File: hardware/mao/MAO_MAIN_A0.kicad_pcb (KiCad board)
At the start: 4 copper layers, 58 x 55.4 mm, 142 parts, among them J101 USB-C, J102 BAT, J201 TAG, J301 LCD, J302 TOUCH TOP, J303 TOUCH REAR, J501 LRA, Q101 AO3401A, Q501 AO3400A, SW301 SKQGADE010, U101 TPD2E2U06, U102 BQ24073RGTR, U103 MAX17048G+T10, U104 TPS63802DLAR, U105 TPS22919DCKR, U201 ESP32-S3-WROOM-1-N8R2, U202 TCA6408ARGTR, U301 DRV5012AEDMRR, U302 DRV5012AEDMRR, U303 AW9364DNR, U401 LSM6DSOXTR, U402 VL53L4CDV0DH/1, U403 OPT3004DNPR, U501 MAX98357AETE+T, U502 DRV2605LDGSR, U503 IRM-H638T/TR2

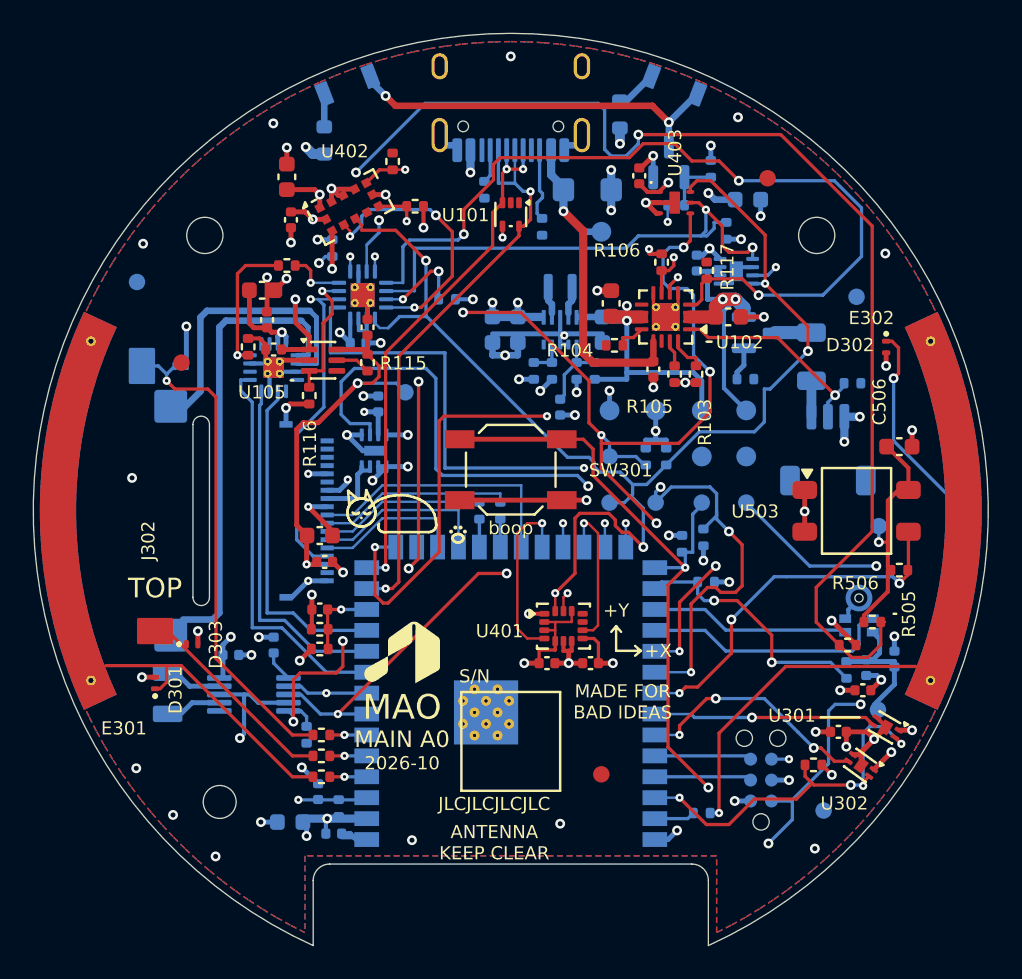
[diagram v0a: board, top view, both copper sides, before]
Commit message: MAO A0 final pass: rebuilt board, panel clock option, doc numbers from the final board
Board (rebuilt from design/, DRC 0 / 0 unconnected / parity 0, planes one piece, silk 0, mech 0):
- silk leaders at least one text height (0.8 mm) long; shorter ones read as dashes
- VSYS via at R502 on the pad's axis: every segment at 0/45/90 degrees
- FAB-NOTES notch size generated from mechanical.py (24.0 mm wide, 7.55 mm deep)
- antenna keep-out comments describe what the rule area really covers

Firmware:
- Kconfig MAO_A0_LCD_PCLK_MHZ (10-80, default 80) for the panel SPI clock through the 70 mm tail
- pin map: BOARD_ID routing note; header regenerated
- all five configurations build with 0 warnings; host tests 240 checks pass

Docs: power budget (EN1 strap 11 uA, deep sleep ~85 uA), mechanical (module datum, notch, wall test,
tabs, tail loop and well, LRA), architecture section 6, factory-test pad positions, firmware merge guide
(clock option, reconfigure note), simulation labels (S3 66 mW at 47 mA, S10 t_ON vs rise, S15 deep sleep),
renders, layer plots, Gerber sheet and assembly previews regenerated.

Co-Authored-By: Claude Opus 5.5 <noreply@anthropic.com>
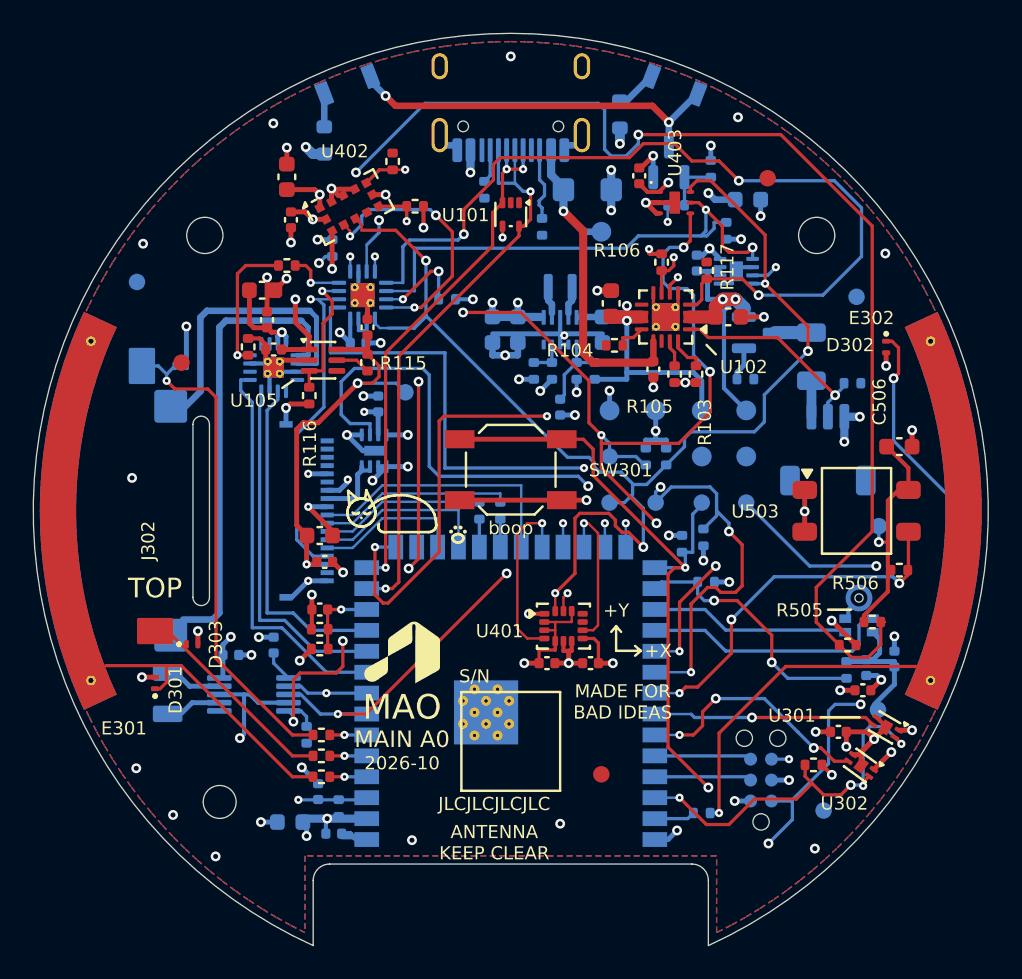
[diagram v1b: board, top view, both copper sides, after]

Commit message: MAO A0 service field: every name upright beside its pad; review and verification docs updated
- mechanical.field_name_box sized to the real glyphs (0.72 mm a character): the router no longer puts a
  via where a name has to go (BOOT was pushed off its pad by one)
- silk.py: field names may use a neighbour's courtyard margin (never its body or pads); the field
  search gets a lower bound and finds the optimum at once (an all-upright set was proved impossible
  before the keep-out change: SYS lay flat)
- check_silk_text.py: the same body rule for field names; findings carry their own position
- TP9's name box slid 0.05 mm clear of the module escape via of LCD_BL_CTRL
- final board: DRC 0 / 0 / parity 0, planes one piece, silk 84 texts 0 findings, mech 0;
  208 vias, 930 segments all on 45 degrees, L3/L4 broadside 17.4 mm
- review: schematic rows (ILIM, GPIO45, board ID), audit-2 change rows 41-52, PCB gates and metrics,
  ODD JOBS and order-readiness rows; verification: summary, S3/S10/S15, second-round section;
  type scale corrected (references 0.8 mm); renders, plots, Gerber sheet regenerated

Co-Authored-By: Claude Opus 5.5 <noreply@anthropic.com>
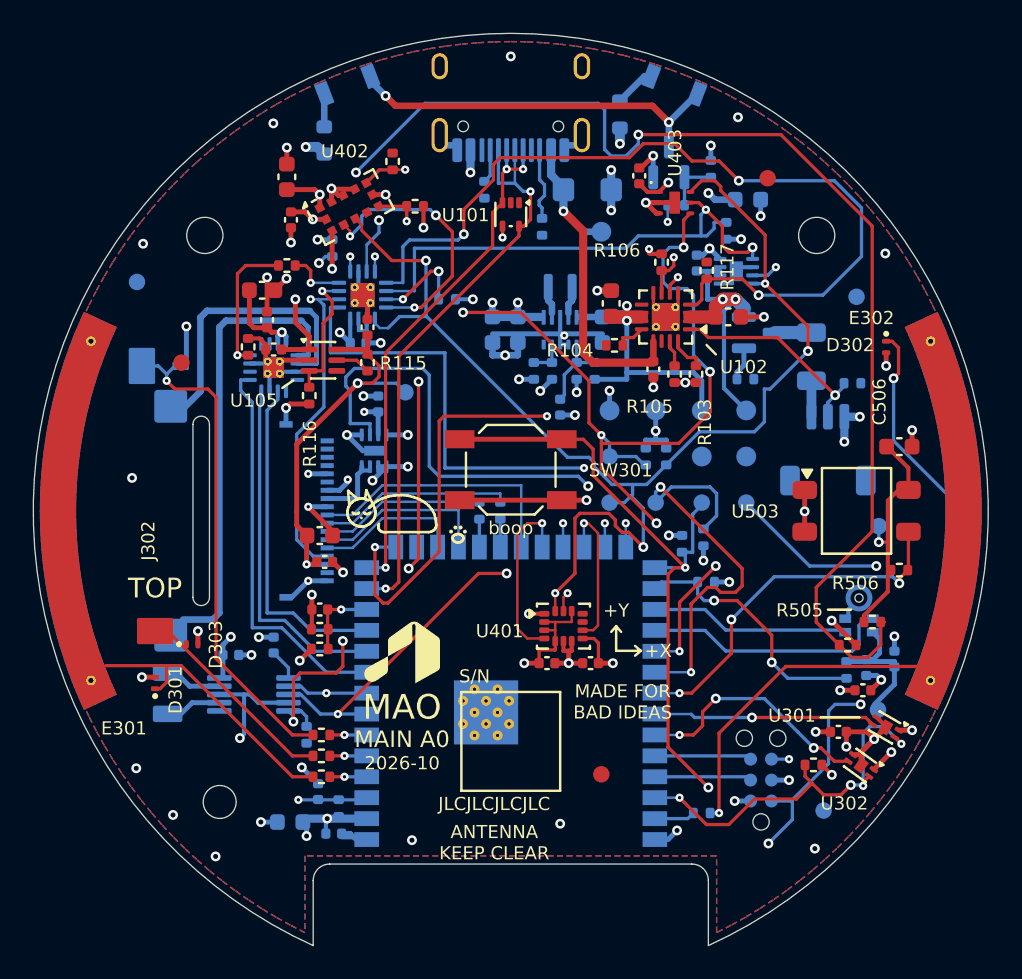
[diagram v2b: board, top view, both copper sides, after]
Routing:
- net EXP_RST_N: track 53.9 -> 56.8 mm, vias 4 -> 3
- net 3V3_LCD: track 24.6 -> 24.1 mm

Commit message: MAO A0 audit 3 fixes: VSYS feed un-necked, speaker lines over VSYS, silk leaders to their parts
Electrical audit 3 (no blocker; issue I-1):
- 11 o'clock panel tab 320 -> 328 deg: its keep-out necked the L3 VSYS band to 0.27 mm beside H1
- via-free corner where the VSYS branch turns into the backlight bar (a C205/U202 via left 0.26 mm)
- plane_check: GND and rail regions refilled at 0.5 mm minimum width must not split (necks fail
  the build); the +3V3 mesh is reported
- self-test board_id upper limit 1700 -> 1720 mV (the 3.32 V rail corner reached 1.697 V)
- comments: rail 3.10-3.32 V, AW9364 dropout, TPS22919 turn-on vs rise, panel clock, Kconfig help
- D101 drawn as a unidirectional TVS (zener glyph); module +3V3 via on C202's branch axis

ODD JOBS audit 3 (0 FAIL; recommended fixes):
- VSYS branch extended under both speaker lines (they sat over the VSYS/+3V3 zone gap); LCD_RST_N
  off L3; L3/L4 broadside 17.4 -> 13.8 mm
- EXP_RST_N's leg to TP11 designed on L3 (left to the router it detoured)
- leaders end 0.3 mm off their own part, at least 0.1 mm nearer it than any other part
- no silk text on touch-electrode copper (silk.py, mao_labels.py, check_silk_text.py): REAR and
  MIC moved
- schematic note lines on a 2.54 mm pitch (snapped 2.29 mm printed pairs that touched); tail note
- back identity on a reserved via-free spot; RSSI check with and without the LRA; drawing text
- final board: DRC 0/0/0, planes whole, no rail neck under 0.5 mm, silk 83 texts 0 findings,
  mech 0, 205 vias, 921 segments on 45 degrees; firmware 5 builds 0 warnings, 240 host checks;
  merge patch re-verified on b17187e

Co-Authored-By: Claude Opus 5.5 <noreply@anthropic.com>
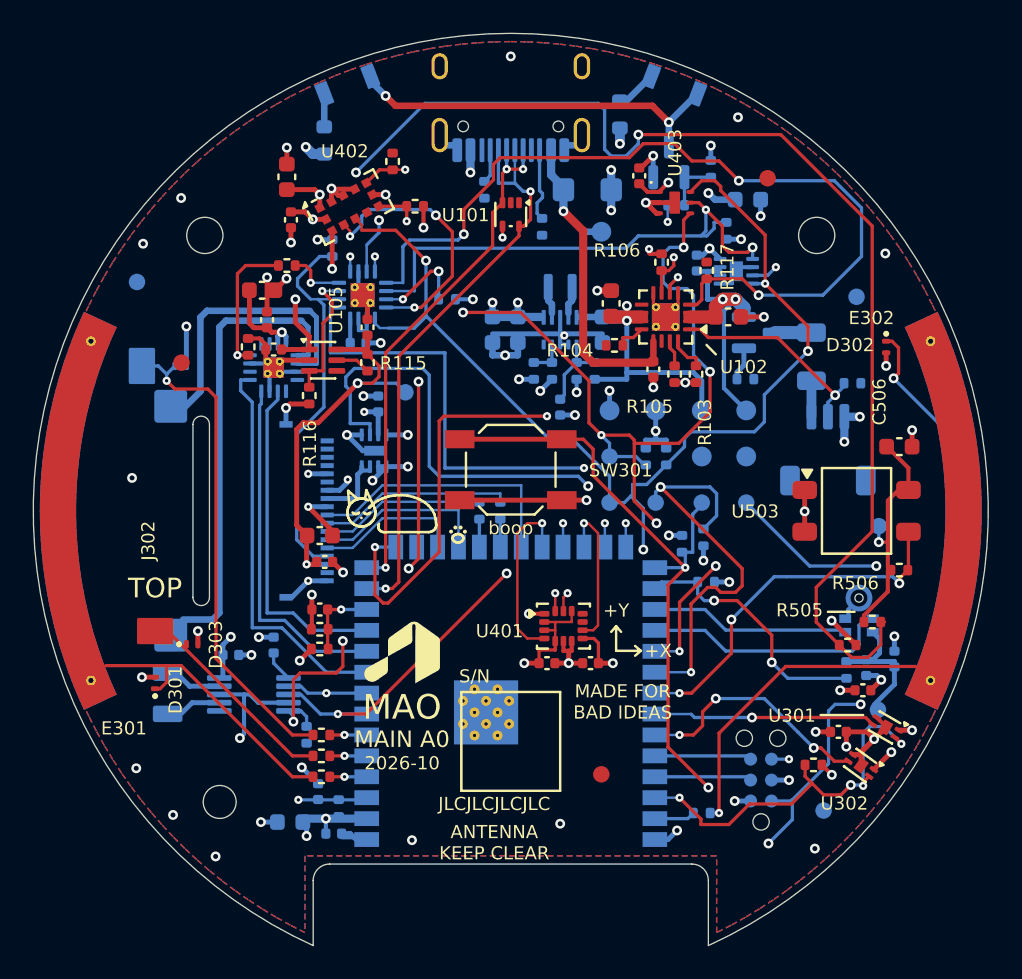
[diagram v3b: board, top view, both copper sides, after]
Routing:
- net LCD_RST_N: track 31.0 -> 23.5 mm, vias 2 -> 0
- net I2C_SDA: track 98.7 -> 95.0 mm
- net I2C_SCL: track 104.4 -> 103.4 mm
- net GND: track 138.5 -> 137.6 mm, vias 74 -> 73
- net EXP_RST_N: track 56.8 -> 56.1 mm
- net 3V3_LCD: track 24.1 -> 24.6 mm
